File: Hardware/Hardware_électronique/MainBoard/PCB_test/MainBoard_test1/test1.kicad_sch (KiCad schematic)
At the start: 0 parts

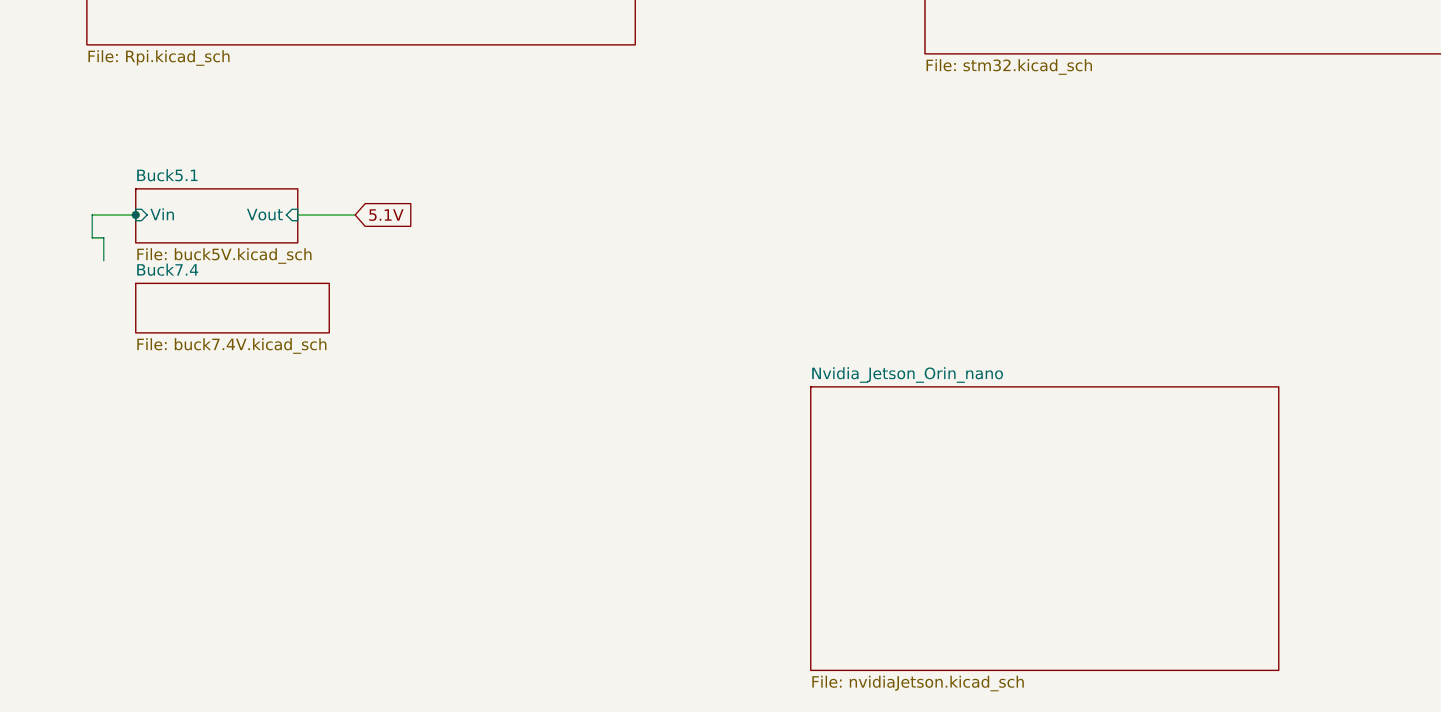
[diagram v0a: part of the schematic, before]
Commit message: Adding motor board
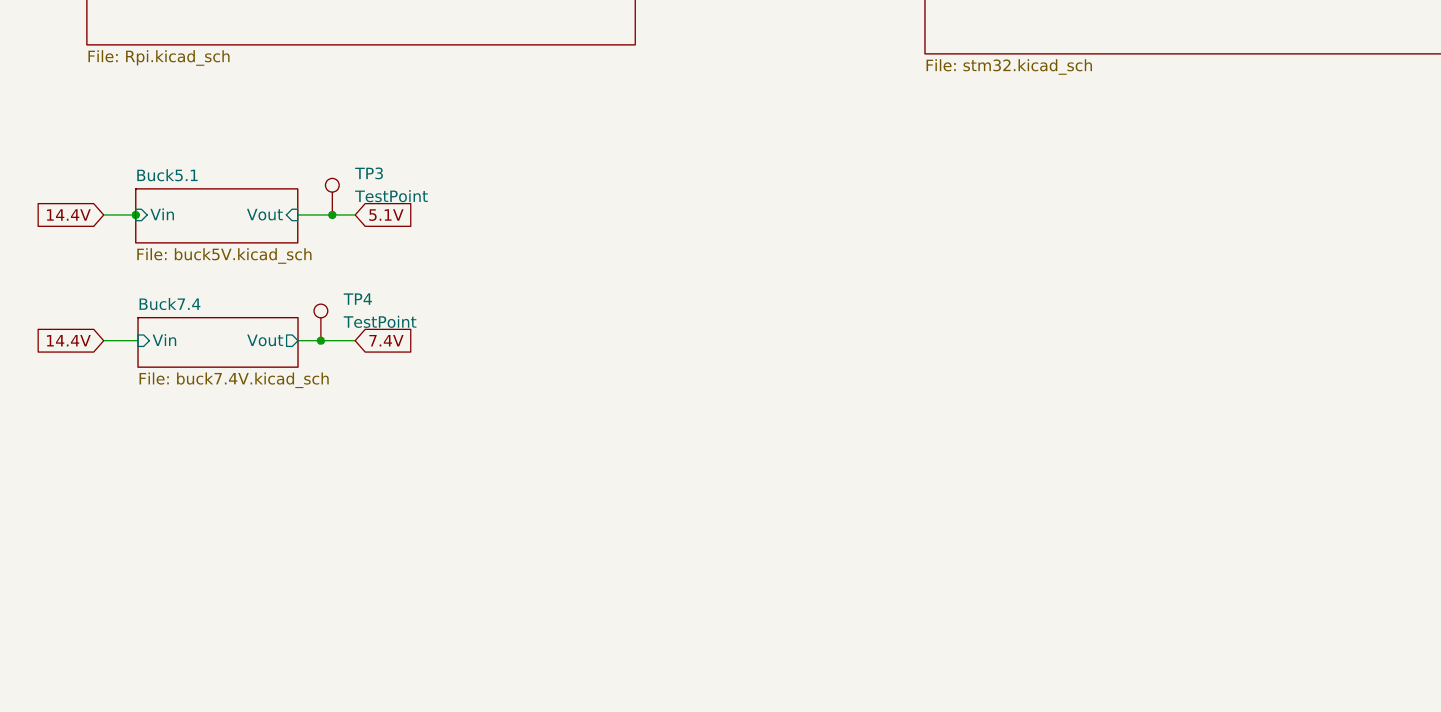
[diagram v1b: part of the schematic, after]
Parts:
- added TP3, TP4: TestPoint, symbol Connector:TestPoint
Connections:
- net 5.1V: now also TP3.1
- new net 7.4V: TP4.1
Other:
- removed sheet Nvidia_Jetson_Orin_nano
- sheet Buck7.4 ports: added Vin, Vout; removed none
